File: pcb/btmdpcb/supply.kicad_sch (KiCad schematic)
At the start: 15 parts, among them J1 USB_C_Receptacle_PowerOnly_6P, Q5 AO3401A, U2 TP4057

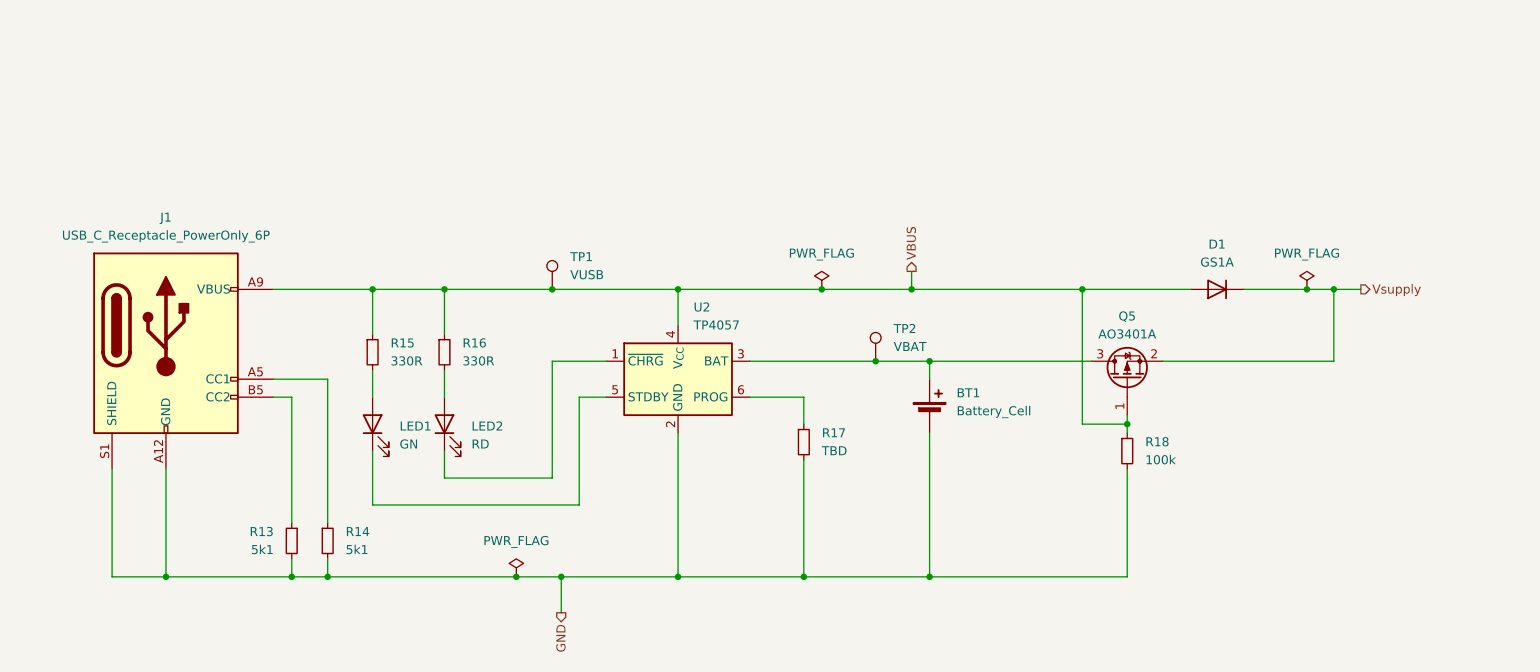
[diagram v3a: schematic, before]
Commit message: Add missing libraries, assign all footprints
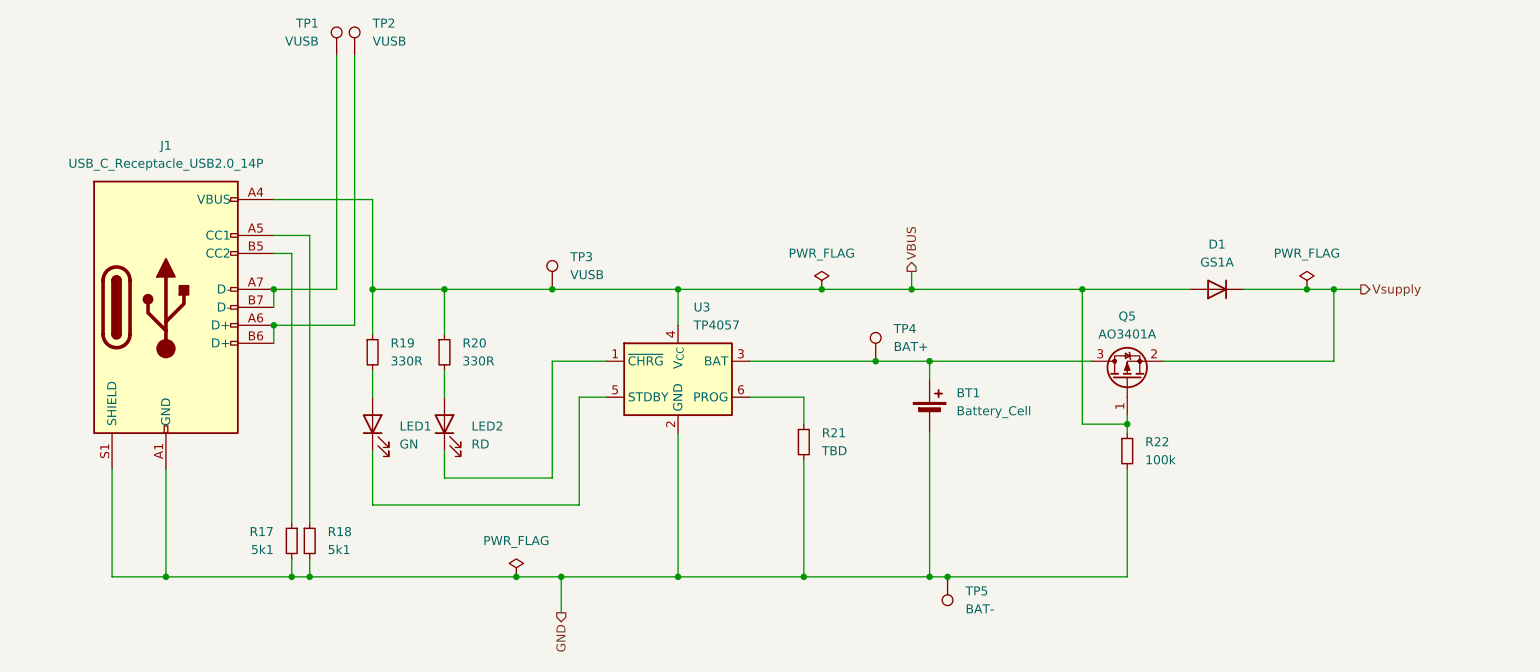
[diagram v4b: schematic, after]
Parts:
- removed J1: USB_C_Receptacle_PowerOnly_6P, symbol Connector:USB_C_Receptacle_PowerOnly_6P
- added J1: USB_C_Receptacle_USB2.0_14P, usb:TYPE-C-31-M-14, symbol Connector:USB_C_Receptacle_USB2.0_14P
- added TP1, TP2: VUSB, TestPoint:TestPoint_Pad_D1.0mm, symbol Connector:TestPoint
- added TP5: BAT-, TestPoint:TestPoint_Pad_D1.0mm, symbol Connector:TestPoint
- D1: footprint (none) -> Diode_SMD:D_SMA
- LED1, LED2: footprint LED_SMD:LED_0603_1608Metric_Pad1.05x0.95mm_HandSolder -> LED_SMD:LED_0805_2012Metric_Pad1.15x1.40mm_HandSolder
- R17: renamed from R13; footprint (none) -> Resistor_SMD:R_0805_2012Metric_Pad1.20x1.40mm_HandSolder
- R18: renamed from R14; footprint (none) -> Resistor_SMD:R_0805_2012Metric_Pad1.20x1.40mm_HandSolder
- R19: renamed from R15; footprint (none) -> Resistor_SMD:R_0805_2012Metric_Pad1.20x1.40mm_HandSolder
- R20: renamed from R16; footprint (none) -> Resistor_SMD:R_0805_2012Metric_Pad1.20x1.40mm_HandSolder
- R21: renamed from R17; footprint (none) -> Resistor_SMD:R_0805_2012Metric_Pad1.20x1.40mm_HandSolder
- R22: renamed from R18; footprint (none) -> Resistor_SMD:R_0805_2012Metric_Pad1.20x1.40mm_HandSolder
- TP3: renamed from TP1; footprint (none) -> TestPoint:TestPoint_Pad_D1.0mm
- TP4: renamed from TP2; value VBAT -> BAT+; footprint (none) -> TestPoint:TestPoint_Pad_D1.0mm
- renumbered U2 to U3
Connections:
- net GND: now also J1.A1 (GND), J1.A12 (GND), J1.B1 (GND), J1.B12 (GND), J1.S1 (SHIELD), TP5.1
- net VBUS: now also J1.A4 (VBUS), J1.A9 (VBUS), J1.B4 (VBUS), J1.B9 (VBUS)
- net at R17.1: now also J1.B5 (CC2)
- net at R18.1: now also J1.A5 (CC1)
- new net: J1.A6 (D+), J1.B6 (D+), TP2.1
- new net: J1.A7 (D-), J1.B7 (D-), TP1.1
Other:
- moved on the sheet: R18

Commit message: Correct footprints, fix issues on update PCB from schematic
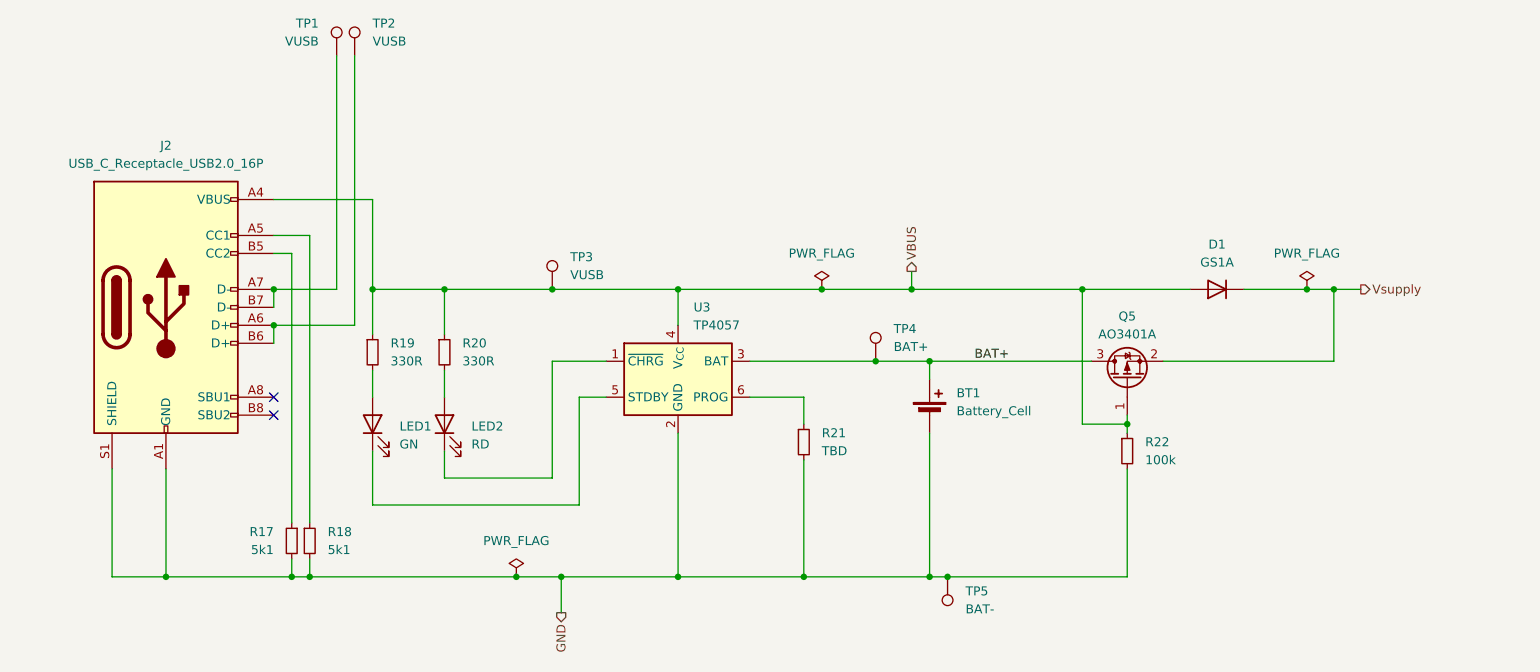
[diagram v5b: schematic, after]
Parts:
- removed J1: USB_C_Receptacle_USB2.0_14P, usb:TYPE-C-31-M-14, symbol Connector:USB_C_Receptacle_USB2.0_14P
- added J2: USB_C_Receptacle_USB2.0_16P, usb:TYPE-C-31-M-14, symbol Connector:USB_C_Receptacle_USB2.0_16P
- D1: footprint Diode_SMD:D_SMA -> Diode_SMD:D_SMA_Handsoldering
- Q5: footprint Package_TO_SOT_SMD:SOT-23 -> Package_TO_SOT_SMD:SOT-23_Handsoldering
- U3: footprint Package_TO_SOT_SMD:TSOT-23-5 -> Package_TO_SOT_SMD:SOT-23-6_Handsoldering
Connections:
- net GND: now also J2.A1 (GND), J2.A12 (GND), J2.B1 (GND), J2.B12 (GND), J2.S1 (SHIELD)
- net VBUS: now also J2.A4 (VBUS), J2.A9 (VBUS), J2.B4 (VBUS), J2.B9 (VBUS)
- net BAT+: now reaches BT1.1 (+), Q5.3 (D), TP4.1, U3.3 (BAT)
- net at TP2.1: now also J2.A6 (D+), J2.B6 (D+)
- net at R17.1: now also J2.B5 (CC2)
- net at R18.1: now also J2.A5 (CC1)
- net at TP1.1: now also J2.A7 (D-), J2.B7 (D-)
- no-connect marks 0 -> 2
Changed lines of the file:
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@@
+	)
+	(junction
+		(at 87.63 63.5)
+		(diameter 0)
+		(color 0 0 0 0)
 	)
 	(junction
@@
 	)
 	(junction
-		(at 87.63 63.5)
-		(diameter 0)
-		(color 0 0 0 0)
-	)
-	(junction
 		(at 144.78 104.14)
 		(diameter 0)
@@
 	)
 	(junction
-		(at 87.63 68.58)
-		(diameter 0)
-		(color 0 0 0 0)
-	)
-	(junction
 		(at 180.34 104.14)
 		(diameter 0)
@@
 	)
 	(junction
+		(at 87.63 68.58)
+		(diameter 0)
+		(color 0 0 0 0)
+	)
+	(junction
 		(at 101.6 63.5)
 		(diameter 0)
@@
 		(color 0 0 0 0)
 	)
+	(no_connect
+		(at 87.63 78.74)
+	)
+	(no_connect
+		(at 87.63 81.28)
+	)
 	(wire
 		(pts
@@
 			(width 0)
 			(type default)
+		)
+	)
+	(label "BAT+"
+		(at 186.69 73.66 0)
+		(fields_autoplaced yes)
+		(effects
+			(font
+				(size 1.27 1.27)
+			)
+			(justify left bottom)
 		)
 	)
@@
 			)
 		)
-		(property "Footprint" "Package_TO_SOT_SMD:SOT-23"
+		(property "Footprint" "Package_TO_SOT_SMD:SOT-23_Handsoldering"
 			(at 210.185 71.12 0)
 			(effects
@@
 			)
 		)
-		(property "Footprint" "Package_TO_SOT_SMD:TSOT-23-5"
+		(property "Footprint" "Package_TO_SOT_SMD:SOT-23-6_Handsoldering"
 			(at 144.78 88.9 0)
 			(effects
@@
 				(path "/6e43e92f-e106-411c-86ee-217d084aee5b/30ff757b-83ca-4184-84db-39f939669bab"
 					(reference "U3")
-					(unit 1)
-				)
-			)
-		)
-	)
-	(symbol
-		(lib_id "Connector:USB_C_Receptacle_USB2.0_14P")
-		(at 72.39 66.04 0)
-		(unit 1)
-		(exclude_from_sim no)
-		(in_bom yes)
-		(on_board yes)
-		(dnp no)
-		(fields_autoplaced yes)
-		(property "Reference" "J1"
-			(at 72.39 43.18 0)
-			(effects
-				(font
-					(size 1.27 1.27)
-				)
-			)
-		)
-		(property "Value" "USB_C_Receptacle_USB2.0_14P"
-			(at 72.39 45.72 0)
-			(effects
-				(font
-					(size 1.27 1.27)
-				)
-			)
-		)
-		(property "Footprint" "usb:TYPE-C-31-M-14"
-			(at 76.2 66.04 0)
-			(effects
-				(font
-					(size 1.27 1.27)
-				)
-				(hide yes)
-			)
-		)
-		(property "Datasheet" "https://www.usb.org/sites/default/files/documents/usb_type-c.zip"
-			(at 76.2 66.04 0)
-			(effects
-				(font
-					(size 1.27 1.27)
-				)
-				(hide yes)
-			)
-		)
-		(property "Description" "USB 2.0-only 14P Type-C Receptacle connector"
-			(at 72.39 66.04 0)
-			(effects
-				(font
-					(size 1.27 1.27)
-				)
-				(hide yes)
-			)
-		)
-		(pin "B1"
-		)
-		(pin "A9"
-		)
-		(pin "B9"
-		)
-		(pin "A1"
-		)
-		(pin "A6"
-		)
-		(pin "B6"
-		)
-		(pin "B12"
-		)
-		(pin "B7"
-		)
-		(pin "A5"
-		)
-		(pin "A4"
-		)
-		(pin "B4"
-		)
-		(pin "S1"
-		)
-		(pin "A7"
-		)
-		(pin "A12"
-		)
-		(pin "B5"
-		)
-		(instances
-			(project ""
-				(path "/6e43e92f-e106-411c-86ee-217d084aee5b/30ff757b-83ca-4184-84db-39f939669bab"
-					(reference "J1")
 					(unit 1)
 				)
@@
 			)
 		)
-		(property "Footprint" "Diode_SMD:D_SMA"
+		(property "Footprint" "Diode_SMD:D_SMA_Handsoldering"
 			(at 220.98 63.5 0)
 			(effects
@@
 					(unit 1)
 				)
+			)
+		)
+	)
+	(symbol
+		(lib_id "Connector:USB_C_Receptacle_USB2.0_16P")
+		(at 72.39 66.04 0)
+		(unit 1)
+		(exclude_from_sim no)
+		(in_bom yes)
+		(on_board yes)
+		(dnp no)
+		(fields_autoplaced yes)
+		(property "Reference" "J2"
+			(at 72.39 43.18 0)
+			(effects
+				(font
+					(size 1.27 1.27)
+				)
+			)
+		)
+		(property "Value" "USB_C_Receptacle_USB2.0_16P"
+			(at 72.39 45.72 0)
+			(effects
+				(font
+					(size 1.27 1.27)
+				)
+			)
+		)
+		(property "Footprint" "usb:TYPE-C-31-M-14"
+			(at 76.2 66.04 0)
+			(effects
+				(font
+					(size 1.27 1.27)
+				)
+				(hide yes)
+			)
+		)
+		(property "Datasheet" "https://www.usb.org/sites/default/files/documents/usb_type-c.zip"
+			(at 76.2 66.04 0)
+			(effects
+				(font
+					(size 1.27 1.27)
+				)
+				(hide yes)
+			)
+		)
+		(property "Description" "USB 2.0-only 16P Type-C Receptacle connector"
+			(at 72.39 66.04 0)
+			(effects
+				(font
+					(size 1.27 1.27)
+				)
+				(hide yes)
+			)
+		)
+		(pin "B5"
+		)
+		(pin "B12"
+		)
+		(pin "B7"
+		)
+		(pin "A7"
+		)
+		(pin "B6"
+		)
+		(pin "A5"
+		)
+		(pin "B4"
+		)
+		(pin "S1"
+		)
+		(pin "B1"
+		)
+		(pin "B9"
+		)
+		(pin "A4"
+		)
+		(pin "A9"
+		)
+		(pin "A8"
+		)
+		(pin "B8"
+		)
+		(pin "A1"
+		)
+		(pin "A6"
+		)
+		(pin "A12"
+		)
+		(instances
+			(project ""
+				(path "/6e43e92f-e106-411c-86ee-217d084aee5b/30ff757b-83ca-4184-84db-39f939669bab"
+					(reference "J2")
+					(unit 1)
+				)

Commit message: Layout PCB
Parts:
- added C3, C4: 10u, Capacitor_SMD:C_0805_2012Metric_Pad1.18x1.45mm_HandSolder, symbol Device:C
- added JP7: SHLD2GND, Jumper:SolderJumper-2_P1.3mm_Open_RoundedPad1.0x1.5mm, symbol Jumper:SolderJumper_2_Open
- added TP3: GND, TestPoint:TestPoint_Pad_D1.0mm, symbol Connector:TestPoint
- added TP7: VSUPPLY, TestPoint:TestPoint_Pad_D1.0mm, symbol Connector:TestPoint
- R19: renamed from R21; value TBD -> 1k6
- TP1: value VUSB -> D-
- TP2: value VUSB -> D+
- TP5: renamed from TP4; value BAT+ -> +
- TP6: renamed from TP5; value BAT- -> -
- renumbered J2 to J1, R17 to R15, R18 to R16, R19 to R17, R20 to R18, R22 to R20, TP3 to TP4, U3 to U2
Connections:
- net BAT+: now also C4.1
- net GND: now also C3.2, C4.2, JP7.2 (B), TP3.1; no longer J1.S1 (SHIELD)
- net VBUS: now also C3.1
- net Vsupply: now also TP7.1
- net D+: now reaches J1.A6 (D+), J1.B6 (D+), TP2.1
- net CC2: now reaches J1.B5 (CC2), R15.1
- net D-: now reaches J1.A7 (D-), J1.B7 (D-), TP1.1
- net CC1: now reaches J1.A5 (CC1), R16.1
- new net SHIELD: J1.S1 (SHIELD), JP7.1 (A)
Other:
- note added: "R[Ω] I[mA] 20k 50 10k 100 5k 200 4k 250 3k 300 2k 400 1k6 500"
- moved on the sheet: BT1, D1, LED1, LED2, R17, R18, R19, TP4, TP5, TP6

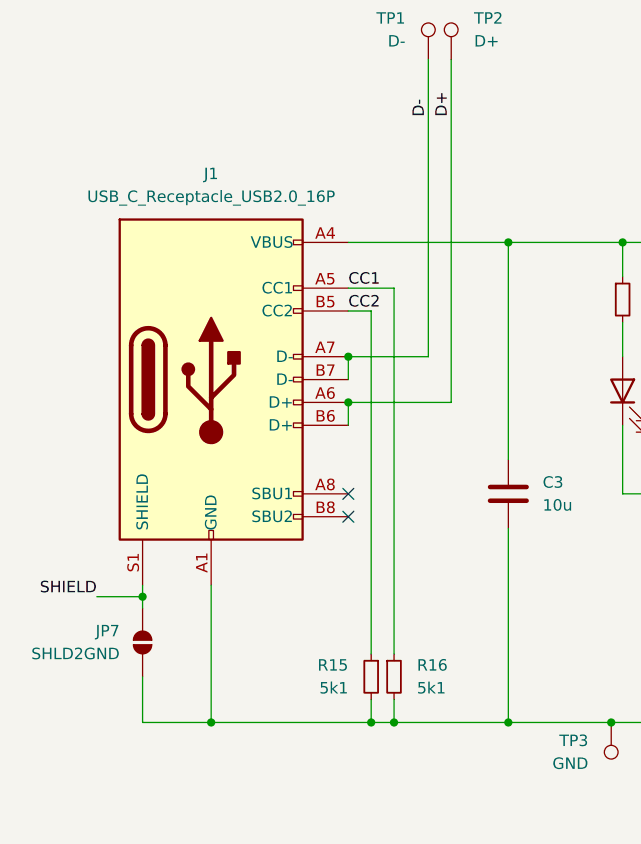
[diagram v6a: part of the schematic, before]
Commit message: Fix connectors & clearance; touch up PCB
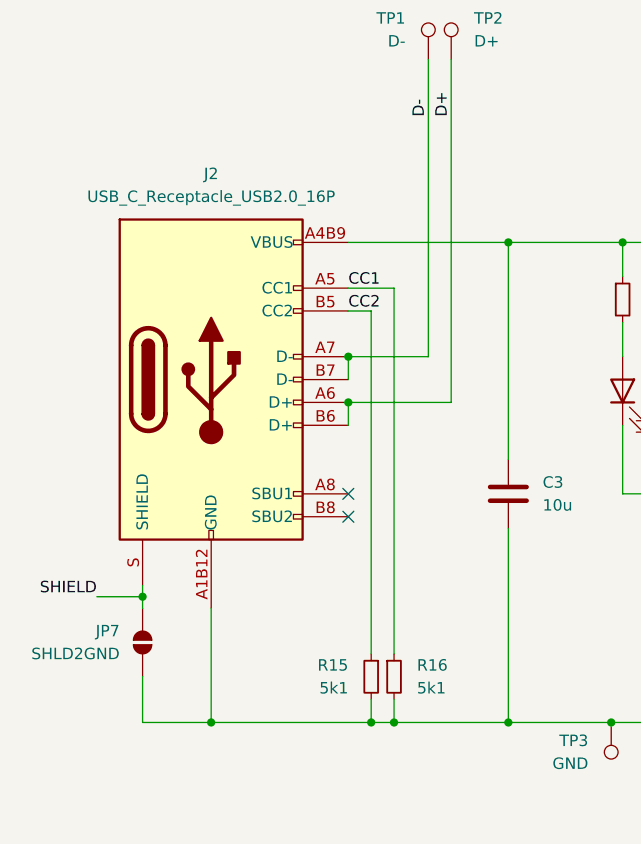
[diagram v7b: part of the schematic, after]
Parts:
- J2: renamed from J1; footprint usb:TYPE-C-31-M-14 -> usb:USB-C-SMD_12P-P0.50-H-F_TYPE-C-31-M-14
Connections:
- net GND: now also J2.A1B12 (GND), J2.B1A12 (GND); no longer J2.A1 (GND), J2.A12 (GND), J2.B1 (GND), J2.B12 (GND)
- net SHIELD: now also J2.S (SHIELD); no longer J2.S1 (SHIELD)
- net VBUS: now also J2.A4B9 (VBUS), J2.B4A9 (VBUS); no longer J2.A4 (VBUS), J2.A9 (VBUS), J2.B4 (VBUS), J2.B9 (VBUS)
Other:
- moved on the sheet: J2
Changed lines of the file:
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@@
+	(wire
+		(pts
+			(xy 72.39 104.14) (xy 72.39 91.44)
+		)
+		(stroke
+			(width 0)
+			(type default)
+		)
+	)
 	(wire
 		(pts
@@
 		(pts
 			(xy 96.52 63.5) (xy 87.63 63.5)
-		)
-		(stroke
-			(width 0)
-			(type default)
-		)
-	)
-	(wire
-		(pts
-			(xy 72.39 104.14) (xy 72.39 88.9)
 		)
 		(stroke
@@
 		(dnp no)
 		(fields_autoplaced yes)
-		(property "Reference" "J1"
+		(property "Reference" "J2"
 			(at 72.39 43.18 0)
 			(effects
@@
 			)
 		)
-		(property "Footprint" "usb:TYPE-C-31-M-14"
+		(property "Footprint" "usb:USB-C-SMD_12P-P0.50-H-F_TYPE-C-31-M-14"
 			(at 76.2 66.04 0)
 			(effects
@@
 		(pin "B5"
 		)
-		(pin "B12"
+		(pin "A4B9"
 		)
 		(pin "B7"
@@
 		(pin "A5"
 		)
-		(pin "B4"
-		)
-		(pin "S1"
-		)
-		(pin "B1"
-		)
-		(pin "B9"
-		)
-		(pin "A4"
-		)
-		(pin "A9"
+		(pin "A1B12"
+		)
+		(pin "S"
+		)
+		(pin "B1A12"
+		)
+		(pin "B4A9"
 		)
 		(pin "A8"
@@
 		(pin "B8"
 		)
-		(pin "A1"
-		)
 		(pin "A6"
 		)
-		(pin "A12"
-		)
 		(instances
 			(project ""
 				(path "/6e43e92f-e106-411c-86ee-217d084aee5b/30ff757b-83ca-4184-84db-39f939669bab"
-					(reference "J1")
-					(unit 1)
-				)
+					(reference "J2")
+					(unit 1)
+				)
